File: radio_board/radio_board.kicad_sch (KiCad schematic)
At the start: 86 parts, among them CN1 HX JN1.27-2X5P ZZ H4.9, Q1 2N7002K, SW2 RKB2SJG250SMTRLFS, SW3 MSK12C02, U1 FSC-BT1036C, U2 TP4057, U3 XB5352A, U4 SKB369, U5 S2B-PH-K-S(LF)(SN), U6 XC6206P332MR

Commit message: [Feature] WIP radio board
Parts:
- added C14: 1nF, Capacitor_SMD:C_0603_1608Metric_Pad1.08x0.95mm_HandSolder, symbol Device:C
- added C15: 1uF, Capacitor_SMD:C_0603_1608Metric_Pad1.08x0.95mm_HandSolder, symbol Device:C
- added C16: 100 nF, Resistor_SMD:R_0603_1608Metric_Pad0.98x0.95mm_HandSolder, symbol Device:C
- added C17, C18, C19, C20: 1uF, Resistor_SMD:R_0603_1608Metric_Pad0.98x0.95mm_HandSolder, symbol Device:C
- added R10, R11, R12, R13, R14, R15: 10k, Resistor_SMD:R_0603_1608Metric_Pad0.98x0.95mm_HandSolder, symbol Device:R
- added TP49: MIC0_LN, TestPoint:TestPoint_THTPad_D2.0mm_Drill1.0mm, symbol Connector:TestPoint
- added TP50: K_CONNECTOR_MIC_IN, TestPoint:TestPoint_THTPad_D2.0mm_Drill1.0mm, symbol Connector:TestPoint
- added TP51: K_CONNECTOR_MIC_IN, TestPoint:TestPoint_Pad_D3.0mm, symbol Connector:TestPoint
- added U7: LMV321, Package_TO_SOT_SMD:SOT-23-5_HandSoldering, symbol Amplifier_Operational:LMV321
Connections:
- net +3.3V: now also C16.2, C17.2, R13.2, U7.5 (V+)
- net GND: now also C14.1, C15.1, C16.1, C17.1, R12.1, U7.2 (V-); no longer U1.44 (MIC0_LN)
- net MIC0_LP: now also C13.2; no longer C13.1
- net SPK_LN: now also C19.2
- net SPK_LP: now also C18.2; no longer C10.1
- net at RV2.2: now also C13.1, C14.2; no longer C13.2
- new net: C18.1, R10.1
- new net: R10.2, R14.1, U7.1 (+)
- new net: R11.2, R15.1, U7.3 (-)
- new net: C20.1, R15.2, U7.4
- new net: C20.2, TP50.1, TP51.1
- new net: R12.2, R13.1, R14.2
- new net: C19.1, R11.1
- new net MIC0_LN: C15.2, TP49.1, U1.44 (MIC0_LN)
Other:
- moved on the sheet: C1, C10, C11, C12, C13, C2, CN1, D1, R1, R7, R8, RV1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

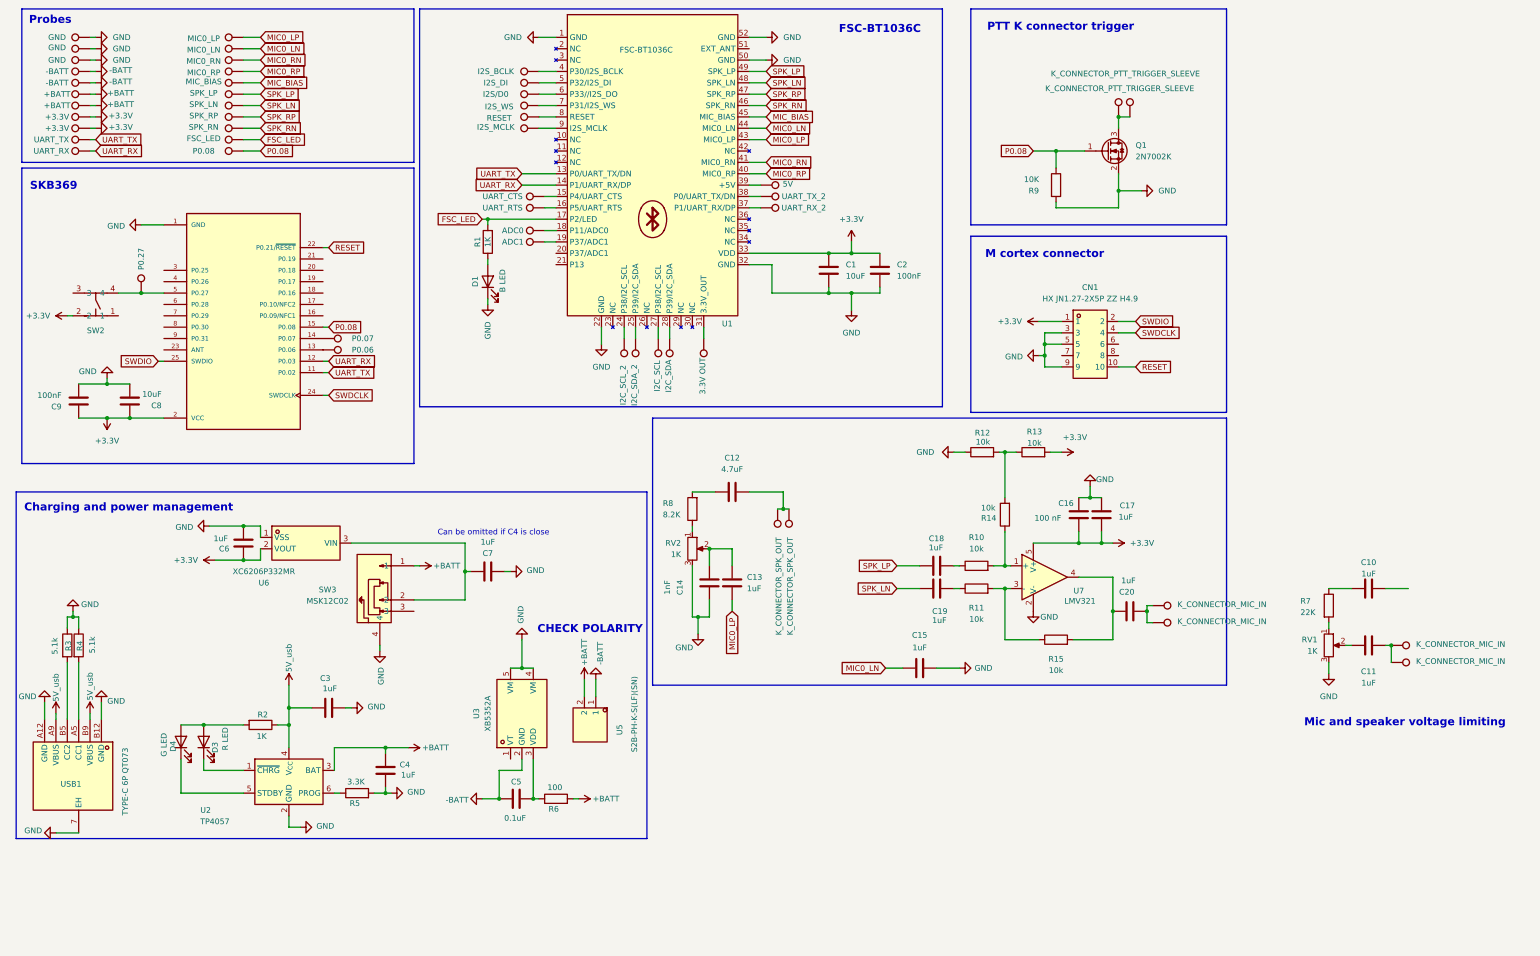
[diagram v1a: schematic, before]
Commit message: [feature fix] Add a proper op amp for radio module
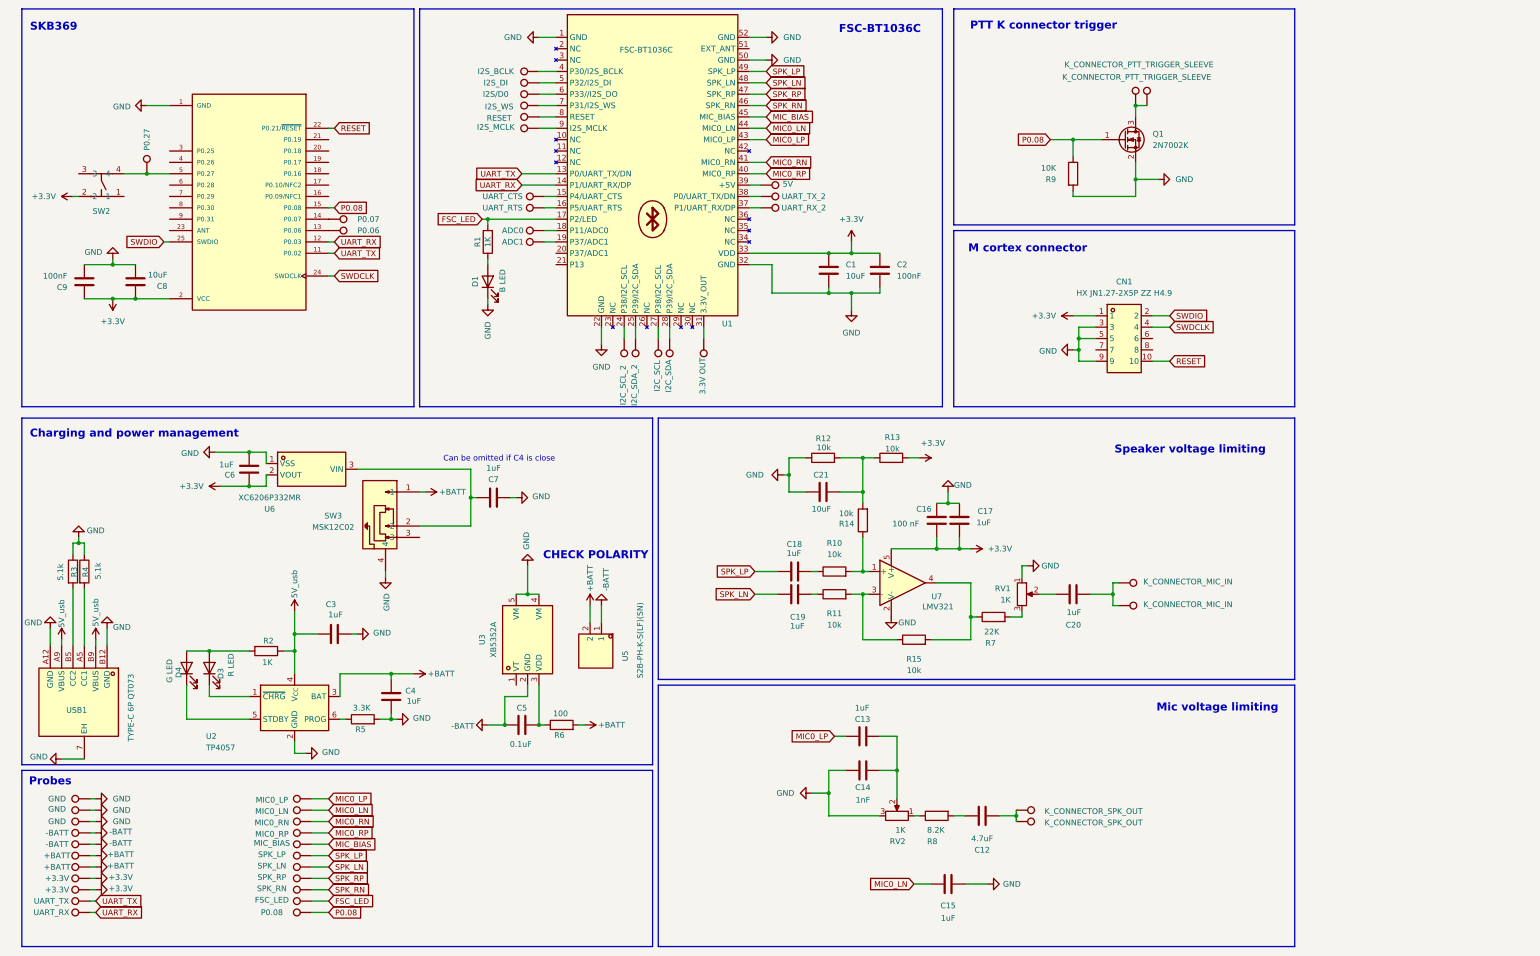
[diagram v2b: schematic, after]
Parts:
- removed C10, C11: 1uF, Resistor_SMD:R_0603_1608Metric_Pad0.98x0.95mm_HandSolder, symbol Device:C
- removed TP37: K_CONNECTOR_MIC_IN, TestPoint:TestPoint_Pad_D3.0mm, symbol Connector:TestPoint
- removed TP44: K_CONNECTOR_MIC_IN, TestPoint:TestPoint_THTPad_D2.0mm_Drill1.0mm, symbol Connector:TestPoint
- added C21: 10uF, Resistor_SMD:R_0603_1608Metric_Pad0.98x0.95mm_HandSolder, symbol Device:C
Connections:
- net GND: now also RV1.1, C21.1; no longer RV1.3
- net at R15.2, U7.4: now also R7.1; no longer C20.1
- net at R7.2: now also RV1.3; no longer RV1.1
- net at R12.2, R13.1, R14.2: now also C21.2
- net at RV1.2: now also C20.1
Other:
- note added: "Mic voltage limiting"
- note added: "Speaker voltage limiting"
- note removed: "Mic and speaker voltage limiting"
- moved on the sheet: C12, C13, C14, C15, C16, C17, C18, C19, C20, C3, C4, C5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

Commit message: [Feature] Rework pcb, better ldo, more filtering
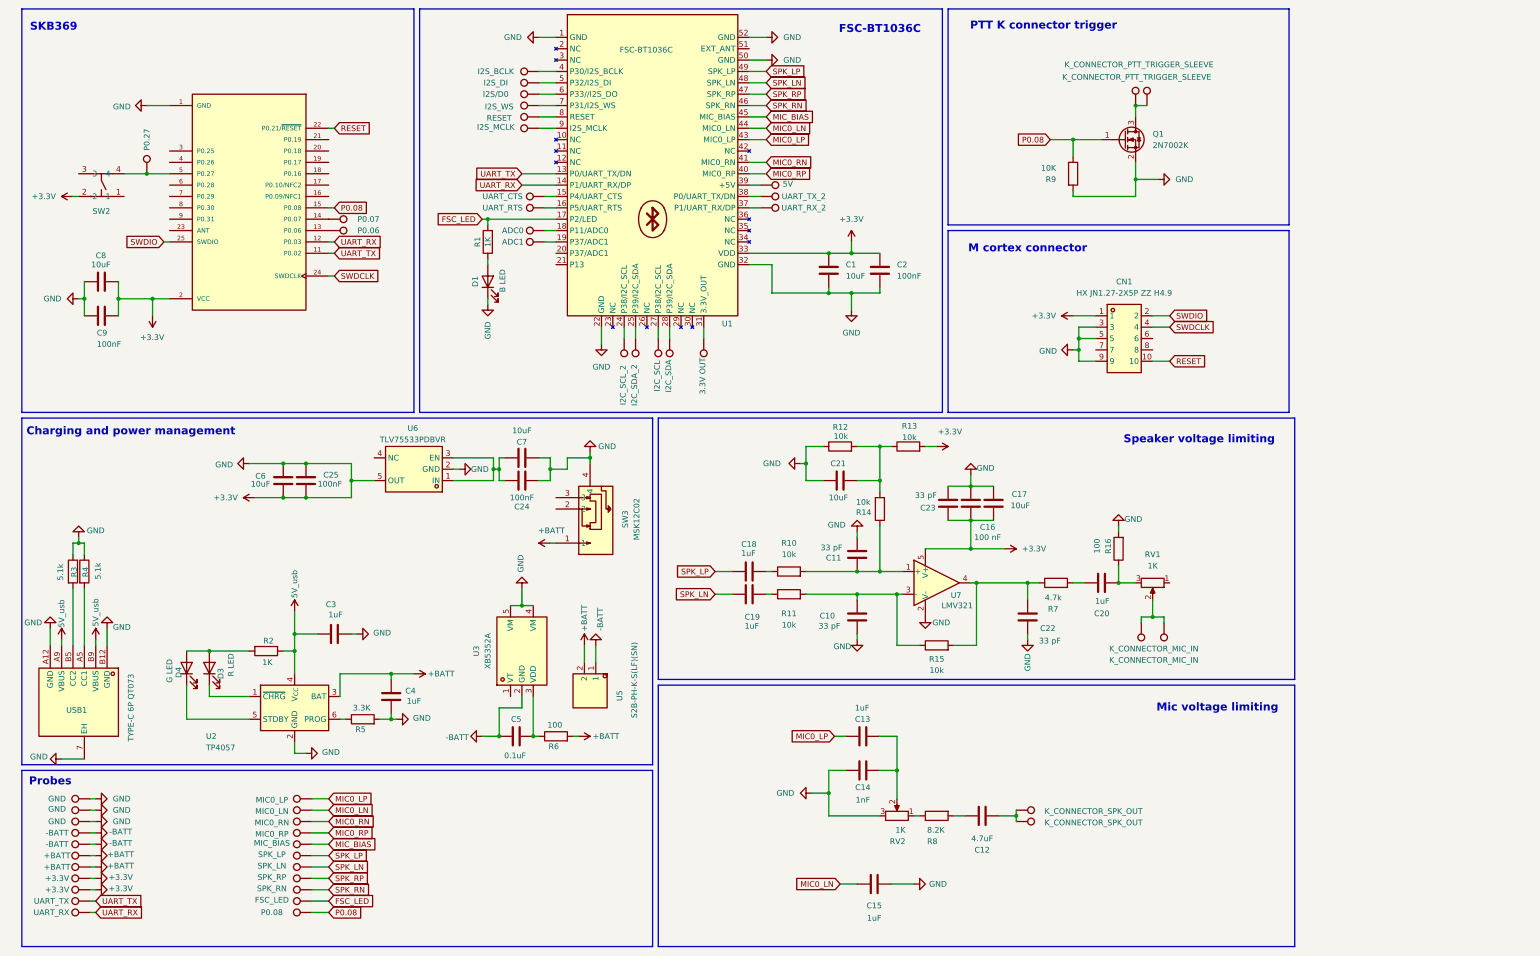
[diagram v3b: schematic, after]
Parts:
- removed U6: XC6206P332MR, Package_TO_SOT_SMD:TSOT-23, symbol PTT_project:XC6206P332MR_C2909968
- added C10, C11, C22, C23: 33 pF, Resistor_SMD:R_0603_1608Metric_Pad0.98x0.95mm_HandSolder, symbol Device:C
- added C24, C25: 100nF, Resistor_SMD:R_0603_1608Metric_Pad0.98x0.95mm_HandSolder, symbol Device:C
- added R16: 100, Resistor_SMD:R_0603_1608Metric_Pad0.98x0.95mm_HandSolder, symbol Device:R
- added U6: TLV75533PDBVR, Project_components:SOT-23-5_L3.0-W1.7-P0.95-LS2.8-BR, symbol PTT_project:TLV75533PDBVR
- C17, C6, C7: value 1uF -> 10uF
- R7: value 22K -> 4.7k
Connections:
- net +3.3V: now also C1.1, C14.1, C15.1, C16.1, C17.1, C2.1, C21.1, C3.1, C4.2, C6.2, C7.1, C8.1, C9.1, CN1.3, CN1.5, CN1.9, D1.1 (K), Q1.2 (S), R12.1, R3.1, R4.1, R5.2, R9.2, RV2.3, SW3.4, TP42.1, TP46.1, TP5.1, U1.1 (GND), U1.22 (GND), U1.32 (GND), U1.50 (GND), U1.52 (GND), U2.2 (GND), U3.4 (VM), U3.5 (VM), U4.1 (GND), U4.10 (GND), U7.2 (V-), USB1.7 (EH), USB1.A12 (GND), USB1.B12 (GND), C10.2, C11.2, C22.1, C23.1, C23.2, C24.1, C25.1, C25.2, R16.2, U6.2 (GND), U6.5 (OUT)
- net at R10.2, R14.1, U7.1 (+): now also C11.1
- net at R11.2, R15.1, U7.3 (-): now also C10.1
- net at R15.2, R7.1, U7.4: now also C22.2
- net at C20.1: now also R7.2; no longer RV1.2
- net at TP50.1, TP51.1: now also RV1.2; no longer C20.2
- net at RV1.3: now also C20.2, R16.1; no longer R7.2
- net at C7.2: now also C24.2, U6.1 (IN), U6.3 (EN); no longer SW3.2
- removed net GND: C1.1, C14.1, C15.1, C16.1, C17.1, C2.1, C21.1, C3.1, C4.2, C6.2, C7.1, C8.1, C9.1, CN1.3, CN1.5, CN1.9, D1.1 (K), Q1.2 (S), R12.1, R3.1, R4.1, R5.2, R9.2, RV1.1, RV2.3, SW3.4, TP42.1, TP46.1, TP5.1, U1.1 (GND), U1.22 (GND), U1.32 (GND), U1.50 (GND), U1.52 (GND), U2.2 (GND), U3.4 (VM), U3.5 (VM), U4.1 (GND), U4.10 (GND), U7.2 (V-), USB1.7 (EH), USB1.A12 (GND), USB1.B12 (GND)
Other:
- note removed: "CHECK POLARITY"
- note removed: "Can be omitted if C4 is close"
- moved on the sheet: C15, C16, C17, C18, C19, C20, C21, C5, C7, C8, C9, R10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

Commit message: [WIP] Started net rev of ptt board and radio board
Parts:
- added C26: 1uF, Resistor_SMD:R_0603_1608Metric_Pad0.98x0.95mm_HandSolder, symbol Device:C
- added C27, C29: 100nF, Resistor_SMD:R_0603_1608Metric_Pad0.98x0.95mm_HandSolder, symbol Device:C
- added C28: 1nF, Resistor_SMD:R_0603_1608Metric_Pad0.98x0.95mm_HandSolder, symbol Device:C
- added D2: RB521S-30_C727120, Project_components:SOD-523_L1.2-W0.8-LS1.6-RD, symbol PTT_project:RB521S-30_C727120
- added L1: BLM18KG601SN1D, Project_components:L0603, symbol PTT_project:BLM18KG601SN1D
- added R17: 470k, Resistor_SMD:R_0603_1608Metric_Pad0.98x0.95mm_HandSolder, symbol Device:R
- added TP37: RESET_SKB, TestPoint:TestPoint_THTPad_D2.0mm_Drill1.0mm, symbol Connector:TestPoint
- added TP44: P0.30, TestPoint:TestPoint_THTPad_D2.0mm_Drill1.0mm, symbol Connector:TestPoint
- added TP52: P0.31, TestPoint:TestPoint_THTPad_D2.0mm_Drill1.0mm, symbol Connector:TestPoint
- R10, R11: value 10k -> 47k
- TP22: value RESET -> RESET_FSC
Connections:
- net +3.3V: now also C27.1, C28.2, C29.2, R17.1
- net RESET: no longer U4.22 (P0.21/~{RESET})
- net at C12.2, R8.2: now also D2.2 (A)
- net P0.30: now reaches U4.8 (P0.30)
- net P0.30: now also C29.1, D2.1 (K), R17.2, TP44.1
- net P0.31: now reaches U4.9 (P0.31)
- net P0.31: now also TP52.1
- net at C21.2, R12.2, R13.1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: now also C27.2
- net at TP50.1, TP51.1: now also C28.1, L1.2; no longer RV1.2
- net RESET_FSC: now reaches TP22.1, U1.8 (RESET)
- new net: C26.1, RV1.2
- new net: C26.2, L1.1
- new net RESET_SKB: TP37.1, U4.22 (P0.21/~{RESET})
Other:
- note added: "Fixed-gain difference amplifier and attenuator"
- note added: "Mic gain"
- note added: "Radio transmittion detector"
- note removed: "Mic voltage limiting"
- note removed: "Speaker voltage limiting"
- moved on the sheet: C12, C13, C14, C15, C21, R14, R8, RV1, RV2

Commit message: [Housekeeping] Renamed project library
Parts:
- removed TP1: P0.06, TestPoint:TestPoint_THTPad_D2.0mm_Drill1.0mm, symbol Connector:TestPoint
- removed TP10: UART_RX, TestPoint:TestPoint_THTPad_D2.0mm_Drill1.0mm, symbol Connector:TestPoint
- removed TP11: UART_RX_2, TestPoint:TestPoint_THTPad_D2.0mm_Drill1.0mm, symbol Connector:TestPoint
- removed TP12: UART_TX_2, TestPoint:TestPoint_THTPad_D2.0mm_Drill1.0mm, symbol Connector:TestPoint
- removed TP13: MIC_BIAS, TestPoint:TestPoint_THTPad_D2.0mm_Drill1.0mm, symbol Connector:TestPoint
- removed TP15: I2C_SCL_2, TestPoint:TestPoint_THTPad_D2.0mm_Drill1.0mm, symbol Connector:TestPoint
- removed TP16: I2C_SDA_2, TestPoint:TestPoint_THTPad_D2.0mm_Drill1.0mm, symbol Connector:TestPoint
- removed TP17: UART_CTS, TestPoint:TestPoint_THTPad_D2.0mm_Drill1.0mm, symbol Connector:TestPoint
- removed TP18: UART_RTS, TestPoint:TestPoint_THTPad_D2.0mm_Drill1.0mm, symbol Connector:TestPoint
- removed TP19: FSC_LED, TestPoint:TestPoint_THTPad_D2.0mm_Drill1.0mm, symbol Connector:TestPoint
- removed TP21: 5V, TestPoint:TestPoint_THTPad_D2.0mm_Drill1.0mm, symbol Connector:TestPoint
- removed TP22: RESET_FSC, TestPoint:TestPoint_THTPad_D2.0mm_Drill1.0mm, symbol Connector:TestPoint
- removed TP23: I2S_WS, TestPoint:TestPoint_THTPad_D2.0mm_Drill1.0mm, symbol Connector:TestPoint
- removed TP24: I2S/D0, TestPoint:TestPoint_THTPad_D2.0mm_Drill1.0mm, symbol Connector:TestPoint
- removed TP25: I2S_DI, TestPoint:TestPoint_THTPad_D2.0mm_Drill1.0mm, symbol Connector:TestPoint
- removed TP26: I2S_BCLK, TestPoint:TestPoint_THTPad_D2.0mm_Drill1.0mm, symbol Connector:TestPoint
- removed TP27: I2S_MCLK, TestPoint:TestPoint_THTPad_D2.0mm_Drill1.0mm, symbol Connector:TestPoint
- removed TP28: ADC0, TestPoint:TestPoint_THTPad_D2.0mm_Drill1.0mm, symbol Connector:TestPoint
- removed TP29: ADC1, TestPoint:TestPoint_THTPad_D2.0mm_Drill1.0mm, symbol Connector:TestPoint
- removed TP3: P0.08, TestPoint:TestPoint_THTPad_D2.0mm_Drill1.0mm, symbol Connector:TestPoint
- removed TP30: I2C_SCL, TestPoint:TestPoint_THTPad_D2.0mm_Drill1.0mm, symbol Connector:TestPoint
- removed TP31: I2C_SDA, TestPoint:TestPoint_THTPad_D2.0mm_Drill1.0mm, symbol Connector:TestPoint
- removed TP32: 3.3V OUT, TestPoint:TestPoint_THTPad_D2.0mm_Drill1.0mm, symbol Connector:TestPoint
- removed TP35: SPK_RP, TestPoint:TestPoint_THTPad_D2.0mm_Drill1.0mm, symbol Connector:TestPoint
- removed TP36: SPK_RN, TestPoint:TestPoint_THTPad_D2.0mm_Drill1.0mm, symbol Connector:TestPoint
- removed TP37: RESET_SKB, TestPoint:TestPoint_THTPad_D2.0mm_Drill1.0mm, symbol Connector:TestPoint
- removed TP39: MIC0_RN, TestPoint:TestPoint_THTPad_D2.0mm_Drill1.0mm, symbol Connector:TestPoint
- removed TP4: P0.27, TestPoint:TestPoint_THTPad_D2.0mm_Drill1.0mm, symbol Connector:TestPoint
- removed TP40: MIC0_RP, TestPoint:TestPoint_THTPad_D2.0mm_Drill1.0mm, symbol Connector:TestPoint
- removed TP42: GND, TestPoint:TestPoint_THTPad_D2.0mm_Drill1.0mm, symbol Connector:TestPoint
- removed TP46: GND, TestPoint:TestPoint_Pad_D3.0mm, symbol Connector:TestPoint
- removed TP48: -BATT, TestPoint:TestPoint_Pad_D3.0mm, symbol Connector:TestPoint
- removed TP7: +3.3V, TestPoint:TestPoint_THTPad_D2.0mm_Drill1.0mm, symbol Connector:TestPoint
- removed TP8: +BATT, TestPoint:TestPoint_THTPad_D2.0mm_Drill1.0mm, symbol Connector:TestPoint
- removed TP9: UART_TX, TestPoint:TestPoint_THTPad_D2.0mm_Drill1.0mm, symbol Connector:TestPoint
- CN1: footprint PTT_project:CONN-TH_10P-P1.27_HX-JN1.27-2X5P-ZZ-H4.9 -> PTT_Project_library:CONN-TH_10P-P1.27_HX-JN1.27-2X5P-ZZ-H4.9; symbol PTT_project:HXJN1.27-2X5PZZH4.9 -> PTT_Project_library:HXJN1.27-2X5PZZH4.9
- D2: footprint Project_components:SOD-523_L1.2-W0.8-LS1.6-RD -> PTT_Project_library:SOD-523_L1.2-W0.8-LS1.6-RD; symbol PTT_project:RB521S-30_C727120 -> PTT_Project_library:RB521S-30_C727120
- L1: footprint Project_components:L0603 -> PTT_Project_library:L0603; symbol PTT_project:BLM18KG601SN1D -> PTT_Project_library:BLM18KG601SN1D
- SW2: footprint PTT_project:Push button C2927788 -> PTT_Project_library:SW-SMD_4P-L4.2-W3.2-P2.15-LS4.6; symbol PTT_project:RKB2SJG250SMTRLFS -> PTT_Project_library:RKB2SJG250SMTRLFS
- SW3: footprint PTT_project:SW-TH_MSK12C02 -> PTT_Project_library:SW-TH_MSK12C02; symbol PTT_project:MSK12C02 -> PTT_Project_library:MSK12C02
- TP2: value P0.07 -> P0.08
- U1: footprint PTT_project:FSC-BT1036C -> PTT_Project_library:FSC-BT1036C; symbol PTT_project:FSC-BT1036C -> PTT_Project_library:FSC-BT1036C
- U3: symbol PTT_project:XB5352A -> PTT_Project_library:XB5352A
- U4: footprint PTT_project:SKYLAB_SKB369 -> PTT_Project_library:SKYLAB_SKB369; symbol PTT_project:SKB369 -> PTT_Project_library:SKB369
- U5: footprint PTT_project:CONN-TH_S2B-PH-K-S-LF-SN -> PTT_Project_library:CONN-TH_S2B-PH-K-S-LF-SN; symbol PTT_project:S2B-PH-K-S(LF)(SN) -> PTT_Project_library:S2B-PH-K-S(LF)(SN)
- U6: footprint Project_components:SOT-23-5_L3.0-W1.7-P0.95-LS2.8-BR -> PTT_Project_library:SOT-23-5_L3.0-W1.7-P0.95-LS2.8-BR; symbol PTT_project:TLV75533PDBVR -> PTT_Project_library:TLV75533PDBVR
- USB1: footprint PTT_project:USB-C-SMD_TYPE-C-6P-QT073 -> PTT_Project_library:USB-C-SMD_TYPE-C-6P-QT073; symbol PTT_project:TYPE-C6PQT073 -> PTT_Project_library:TYPE-C6PQT073
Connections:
- net P0.08: now also TP2.1
- net at U4.14 (P0.07): no longer TP2.1

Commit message: [WIP]
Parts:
- removed U4: SKB369, PTT_Project_library:SKYLAB_SKB369, symbol PTT_Project_library:SKB369
- added C30, C31: 100nF, Resistor_SMD:R_0603_1608Metric_Pad0.98x0.95mm_HandSolder, symbol Device:C
- added D5: B LED, LED_SMD:LED_0603_1608Metric_Pad1.05x0.95mm_HandSolder, symbol Device:LED
- added R18, R20: 10K, Resistor_SMD:R_0603_1608Metric_Pad0.98x0.95mm_HandSolder, symbol Device:R
- added R19: 1K, Resistor_SMD:R_0603_1608Metric_Pad0.98x0.95mm_HandSolder, symbol Device:R
- added U8: STM32G030F6P6TR, PTT_Project_library:TSSOP-20_L6.5-W4.4-P0.65-LS6.4-BL, symbol PTT_Project_library:STM32G030F6P6TR
- TP2: value P0.08 -> PTT_Trigger
- TP44: value P0.30 -> Squelch_detect
- TP52: value P0.31 -> Debug_gpio
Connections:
- net +3.3V: now also R20.2, U8.4 (VDDA/DDA); no longer C1.1, C10.2, C11.2, C14.1, C15.1, C16.1, C17.1, C2.1, C21.1, C22.1, C23.1, C24.1, C25.1, C27.1, C28.2, C29.2, C3.1, C4.2, C6.1, C7.1, C8.1, C9.1, CN1.3, CN1.5, CN1.9, D1.1 (K), Q1.2 (S), R12.1, R16.2, R17.1, R3.1, R4.1, R5.2, R9.2, RV2.3, SW3.4, TP5.1, U1.1 (GND), U1.22 (GND), U1.32 (GND), U1.50 (GND), U1.52 (GND), U2.2 (GND), U3.4 (VM), U3.5 (VM), U6.2 (GND), U7.2 (V-), USB1.7 (EH), USB1.A12 (GND), USB1.B12 (GND)
- net +BATT: now also U8.12 (PA5)
- net RESET: now also C30.1, U8.6 (NRST)
- net RESET_FSC: now also C31.2, R20.1, U8.9 (PA2)
- net SWDCLK: now also R18.1, U8.19 (PA15/PA14-BOOT0)
- net SWDIO: now also U8.18 (PA13)
- net UART_RX: now also U8.20 (PB3/PB4/PB5/PB6)
- net UART_TX: now also U8.1 (PB7/PB8)
- net at SW2.4: now also U8.11 (PA4)
- net at SW3.2: now also C24.1, C7.1
- net P0.08 renamed PTT_Trigger
- net PTT_Trigger: now also U8.13 (PA6)
- net P0.30 renamed Squelch_detect
- net Squelch_detect: now also U8.14 (PA7)
- net P0.31 renamed Debug_gpio
- net Debug_gpio: now also R19.2, U8.10 (PA3)
- new net: D5.2 (A), R19.1
- new net GND: C1.1, C10.2, C11.2, C14.1, C15.1, C16.1, C17.1, C2.1, C21.1, C22.1, C23.1, C25.1, C27.1, C28.2, C29.2, C3.1, C30.2, C31.1, C4.2, C6.1, C8.1, C9.1, CN1.3, CN1.5, CN1.9, D1.1 (K), D5.1 (K), Q1.2 (S), R12.1, R16.2, R17.1, R18.2, R3.1, R4.1, R5.2, R9.2, RV2.3, SW3.4, TP5.1, U1.1 (GND), U1.22 (GND), U1.32 (GND), U1.50 (GND), U1.52 (GND), U2.2 (GND), U3.4 (VM), U3.5 (VM), U6.2 (GND), U7.2 (V-), U8.5 (VSSA/SSA), USB1.7 (EH), USB1.A12 (GND), USB1.B12 (GND)
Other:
- note added: "STM32"
- note removed: "SKB369"
- moved on the sheet: C1, C10, C11, C12, C13, C14, C15, C16, C17, C18, C19, C2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
